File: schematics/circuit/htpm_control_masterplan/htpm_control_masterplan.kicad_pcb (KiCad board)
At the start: 2 copper layers, 248.9 x 185.4 mm, 380 parts, among them J1 Conn_01x08_Socket, J1 Conn_01x10_Socket, J2 Conn_01x04_Socket, J2 Conn_01x10_Socket, J3 Conn_01x08_Socket

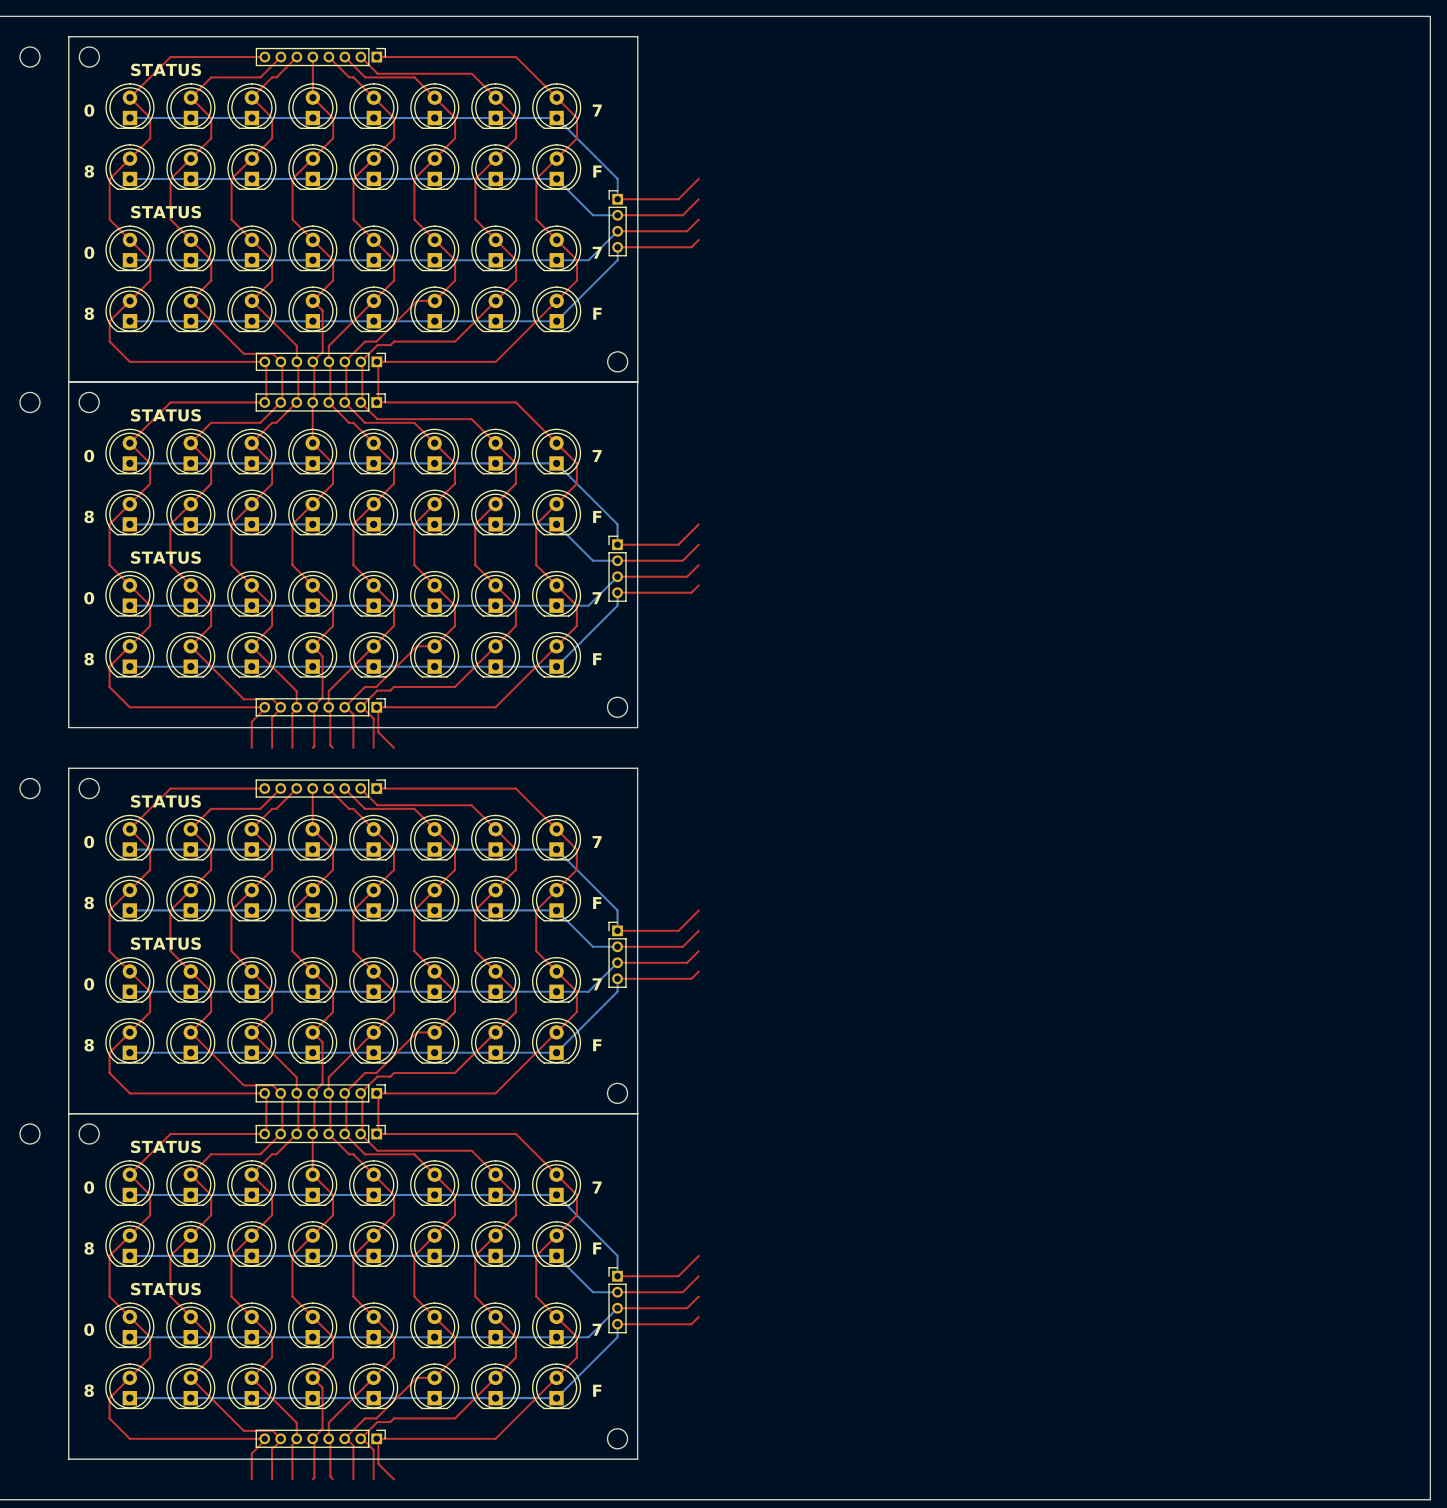
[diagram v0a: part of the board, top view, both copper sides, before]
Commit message: Added HTPm CONTROL Numericals to the masterplan.
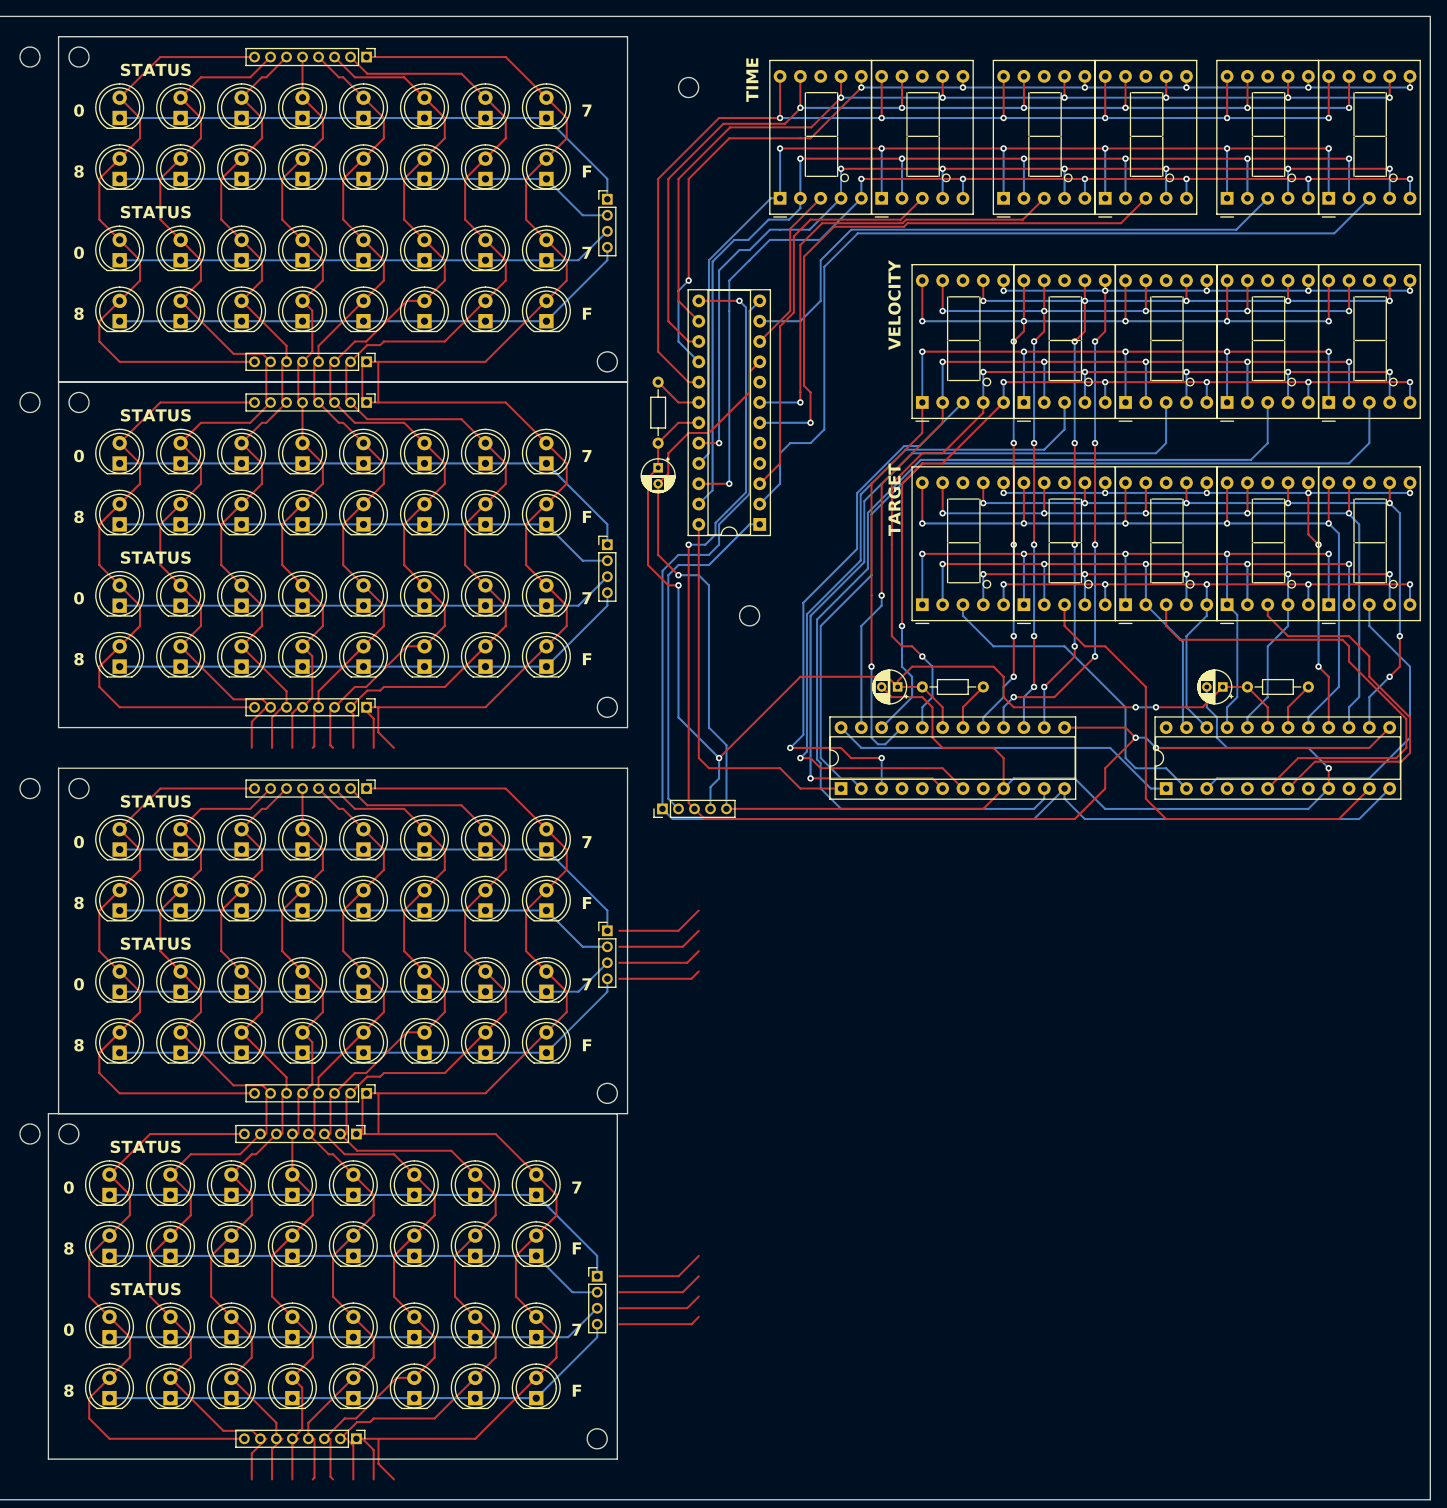
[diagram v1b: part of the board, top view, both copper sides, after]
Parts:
- added C1: 10μF, Capacitor_THT:CP_Radial_D4.0mm_P2.00mm, F.Cu at (238.8, 107.2)
- added C2: 10μF, Capacitor_THT:CP_Radial_D4.0mm_P2.00mm, F.Cu at (268.7, 134.6)
- added C3: 10μF, Capacitor_THT:CP_Radial_D4.0mm_P2.00mm, F.Cu at (309.3, 134.6)
- added H1: MountingHole, MountingHole:MountingHole_2.5mm, F.Cu at (242.6, 59.7)
- added H2: MountingHole, MountingHole:MountingHole_2.5mm, F.Cu at (250.2, 125.7)
- added J1: Conn_01x05_Socket, Connector_PinHeader_2.00mm:PinHeader_1x05_P2.00mm_Vertical, F.Cu at (239.3, 149.9)
- added R1: 15kΩ, Resistor_THT:R_Axial_DIN0204_L3.6mm_D1.6mm_P7.62mm_Horizontal, F.Cu at (238.8, 104.1)
- added R2: 15kΩ, Resistor_THT:R_Axial_DIN0204_L3.6mm_D1.6mm_P7.62mm_Horizontal, F.Cu at (271.8, 134.6)
- added R3: 15kΩ, Resistor_THT:R_Axial_DIN0204_L3.6mm_D1.6mm_P7.62mm_Horizontal, F.Cu at (312.4, 134.6)
- added U1: MAX7219, Package_DIP:DIP-24_W7.62mm_Socket, F.Cu at (251.5, 114.3)
- added U10: D168K, Display_7Segment:D1X8K, F.Cu at (297.2, 99.1)
- added U11: D168K, Display_7Segment:D1X8K, F.Cu at (309.9, 99.1)
- added U12: D168K, Display_7Segment:D1X8K, F.Cu at (322.6, 99.1)
- added U13: MAX7219, Package_DIP:DIP-24_W7.62mm_Socket, F.Cu at (261.6, 147.3)
- added U14: D168K, Display_7Segment:D1X8K, F.Cu at (322.6, 124.3)
- added U15: D168K, Display_7Segment:D1X8K, F.Cu at (309.9, 124.3)
- added U16: D168K, Display_7Segment:D1X8K, F.Cu at (297.2, 124.3)
- added U17: D168K, Display_7Segment:D1X8K, F.Cu at (284.5, 124.3)
- added U18: MAX7219, Package_DIP:DIP-24_W7.62mm_Socket, F.Cu at (302.3, 147.3)
- added U19: D168K, Display_7Segment:D1X8K, F.Cu at (271.8, 124.3)
- added U2: D168K, Display_7Segment:D1X8K, F.Cu at (254.0, 73.5)
- added U3: D168K, Display_7Segment:D1X8K, F.Cu at (266.7, 73.5)
- added U4: D168K, Display_7Segment:D1X8K, F.Cu at (281.9, 73.5)
- added U5: D168K, Display_7Segment:D1X8K, F.Cu at (294.6, 73.5)
- added U6: D168K, Display_7Segment:D1X8K, F.Cu at (309.9, 73.5)
- added U7: D168K, Display_7Segment:D1X8K, F.Cu at (322.6, 73.5)
- added U8: D168K, Display_7Segment:D1X8K, F.Cu at (271.8, 99.1)
- added U9: D168K, Display_7Segment:D1X8K, F.Cu at (284.5, 99.1)
- moved D11 2.54 mm to (185.4, 205.7)
- moved D12 2.54 mm to (193.0, 205.7)
- moved D19 2.54 mm to (185.4, 215.9)
- moved D20 2.54 mm to (193.0, 215.9)
- moved D27 2.54 mm to (185.4, 223.5)
- moved D28 2.54 mm to (193.0, 223.5)
- moved D3 2.54 mm to (185.4, 198.1)
- moved D4 2.54 mm to (193.0, 198.1)
- moved H2 2.54 mm to (231.1, 228.6)
- moved J1 2.54 mm to (201.0, 190.5)
- moved J2 2.54 mm to (231.1, 208.3)
- moved J3 2.54 mm to (201.0, 228.6)
- moved D1 2.54 mm to (170.2, 198.1)
- moved D10 2.54 mm to (177.8, 205.7)
- moved D13 2.54 mm to (200.7, 205.7)
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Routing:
- net (no net): track 8966.2 -> 13677.3 mm, vias 36 -> 211
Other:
- outline, holes or cut-outs redrawn
- board text added: "HTP!m CONTROL Numericals by shawnd.xyz"
- board text added: "TARGET"
- board text added: "TIME"
- board text added: "VELOCITY"

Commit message: Updated masterplan.
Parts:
- removed the C1 at (238.8, 107.2)
- removed the C2 at (268.7, 134.6)
- removed the C3 at (309.3, 134.6)
- removed the D1 at (171.4, 63.5)
- removed the D1 at (119.6, 106.7)
- removed the D1 at (170.2, 198.1)
- removed the D1 at (171.4, 106.7)
- removed the D1 at (119.6, 198.1)
- removed the D1 at (171.4, 154.9)
- removed the D1 at (119.6, 63.5)
- removed the D1 at (119.6, 154.9)
- removed the D10 at (177.8, 205.7)
- removed the D10 at (152.6, 160.0)
- removed the D10 at (152.6, 111.8)
- removed the D10 at (152.6, 203.2)
- removed the D10 at (179.1, 162.6)
- removed the D10 at (179.1, 114.3)
- removed the D10 at (152.6, 68.6)
- removed the D10 at (179.1, 71.1)
- removed the D11 at (186.7, 71.1)
- removed the D11 at (129.8, 81.3)
- removed the D11 at (129.8, 215.9)
- removed the D11 at (129.8, 124.5)
- removed the D11 at (186.7, 114.3)
- removed the D11 at (129.8, 172.7)
- removed the D11 at (185.4, 205.7)
- removed the D11 at (186.7, 162.6)
- removed the D12 at (137.4, 215.9)
- removed the D12 at (193.0, 205.7)
- removed the D12 at (137.4, 172.7)
- removed the D12 at (137.4, 81.3)
- removed the D12 at (137.4, 124.5)
- removed the D12 at (194.3, 162.6)
- removed the D12 at (194.3, 71.1)
- removed the D12 at (194.3, 114.3)
- removed the D13 at (145.0, 124.5)
- removed the D13 at (145.0, 81.3)
- removed the D13 at (145.0, 215.9)
- removed the D13 at (145.0, 172.7)
- removed the D13 at (201.9, 114.3)
- removed the D13 at (201.9, 71.1)
- removed the D13 at (201.9, 162.6)
- removed the D13 at (200.7, 205.7)
- removed the D14 at (208.3, 205.7)
- removed the D14 at (209.6, 162.6)
- removed the D14 at (209.6, 114.3)
- removed the D14 at (209.6, 71.1)
- removed the D14 at (152.6, 172.7)
- removed the D14 at (152.6, 81.3)
- removed the D14 at (152.6, 215.9)
- removed the D14 at (152.6, 124.5)
- removed the D15 at (129.8, 221.0)
- removed the D15 at (217.2, 71.1)
- removed the D15 at (217.2, 114.3)
- removed the D15 at (129.8, 177.8)
- removed the D15 at (215.9, 205.7)
- removed the D15 at (217.2, 162.6)
- removed the D15 at (129.8, 86.4)
- removed the D15 at (129.8, 129.5)
- removed the D16 at (224.8, 71.1)
- removed the D16 at (224.8, 114.3)
- removed the D16 at (137.4, 129.5)
- removed the D16 at (137.4, 221.0)
- removed the D16 at (223.5, 205.7)
- removed the D16 at (137.4, 86.4)
- removed the D16 at (224.8, 162.6)
- removed the D16 at (137.4, 177.8)
- removed the D17 at (145.0, 86.4)
- removed the D17 at (171.4, 172.7)
- removed the D17 at (171.4, 81.3)
- removed the D17 at (145.0, 129.5)
- removed the D17 at (170.2, 215.9)
- removed the D17 at (171.4, 124.5)
- removed the D17 at (145.0, 221.0)
- removed the D17 at (145.0, 177.8)
- removed the D18 at (179.1, 172.7)
- removed the D18 at (177.8, 215.9)
- removed the D18 at (179.1, 81.3)
- removed the D18 at (152.6, 86.4)
- removed the D18 at (152.6, 177.8)
- removed the D18 at (152.6, 129.5)
- removed the D18 at (179.1, 124.5)
- removed the D18 at (152.6, 221.0)
- removed the D19 at (186.7, 81.3)
- removed the D19 at (185.4, 215.9)
- removed the D19 at (186.7, 172.7)
- removed the D19 at (186.7, 124.5)
- removed the D2 at (119.6, 81.3)
- removed the D2 at (179.1, 154.9)
- removed the D2 at (119.6, 124.5)
- removed the D2 at (179.1, 63.5)
- removed the D2 at (119.6, 172.7)
- removed the D2 at (179.1, 106.7)
- removed the D2 at (177.8, 198.1)
- removed the D2 at (119.6, 215.9)
- removed the D20 at (194.3, 172.7)
- removed the D20 at (194.3, 124.5)
- removed the D20 at (194.3, 81.3)
- removed the D20 at (193.0, 215.9)
- removed the D21 at (201.9, 172.7)
- removed the D21 at (200.7, 215.9)
- removed the D21 at (201.9, 81.3)
- removed the D21 at (201.9, 124.5)
- removed the D22 at (209.6, 124.5)
- removed the D22 at (208.3, 215.9)
- removed the D22 at (209.6, 81.3)
- removed the D22 at (209.6, 172.7)
- removed the D23 at (217.2, 81.3)
- removed the D23 at (215.9, 215.9)
- removed the D23 at (217.2, 124.5)
- removed the D23 at (217.2, 172.7)
- removed the D24 at (224.8, 81.3)
- removed the D24 at (224.8, 172.7)
- removed the D24 at (223.5, 215.9)
- removed the D24 at (224.8, 124.5)
- removed the D25 at (170.2, 223.5)
- removed the D25 at (171.4, 88.9)
- removed the D25 at (171.4, 132.1)
- removed the D25 at (171.4, 180.3)
- removed the D26 at (179.1, 180.3)
- removed the D26 at (179.1, 88.9)
- removed the D26 at (177.8, 223.5)
- removed the D26 at (179.1, 132.1)
- removed the D27 at (186.7, 88.9)
- removed the D27 at (185.4, 223.5)
- removed the D27 at (186.7, 132.1)
- removed the D27 at (186.7, 180.3)
- removed the D28 at (194.3, 132.1)
- removed the D28 at (193.0, 223.5)
- removed the D28 at (194.3, 180.3)
- removed the D28 at (194.3, 88.9)
- removed the D29 at (201.9, 180.3)
- removed the D29 at (201.9, 132.1)
- removed the D29 at (201.9, 88.9)
- removed the D29 at (200.7, 223.5)
- removed the D3 at (129.8, 154.9)
- removed the D3 at (186.7, 63.5)
- removed the D3 at (129.8, 63.5)
- removed the D3 at (129.8, 106.7)
- removed the D3 at (129.8, 198.1)
- removed the D3 at (186.7, 154.9)
- removed the D3 at (185.4, 198.1)
- removed the D3 at (186.7, 106.7)
- removed the D30 at (208.3, 223.5)
- removed the D30 at (209.6, 132.1)
- removed the D30 at (209.6, 88.9)
- removed the D30 at (209.6, 180.3)
- removed the D31 at (217.2, 88.9)
- removed the D31 at (217.2, 180.3)
- removed the D31 at (217.2, 132.1)
- removed the D31 at (215.9, 223.5)
- removed the D32 at (224.8, 180.3)
- removed the D32 at (224.8, 132.1)
- removed the D32 at (224.8, 88.9)
- removed the D32 at (223.5, 223.5)
- removed the D4 at (137.4, 154.9)
- removed the D4 at (137.4, 63.5)
- removed the D4 at (194.3, 154.9)
- removed the D4 at (194.3, 63.5)
- removed the D4 at (193.0, 198.1)
- removed the D4 at (194.3, 106.7)
- removed the D4 at (137.4, 198.1)
- removed the D4 at (137.4, 106.7)
- removed the D5 at (201.9, 154.9)
- removed the D5 at (145.0, 198.1)
- removed the D5 at (145.0, 154.9)
- removed the D5 at (145.0, 63.5)
- removed the D5 at (145.0, 106.7)
- removed the D5 at (200.7, 198.1)
- removed the D5 at (201.9, 106.7)
- removed the D5 at (201.9, 63.5)
- removed the D6 at (152.6, 154.9)
- removed the D6 at (209.6, 154.9)
- removed the D6 at (152.6, 198.1)
- removed the D6 at (208.3, 198.1)
- removed the D6 at (209.6, 106.7)
- removed the D6 at (209.6, 63.5)
- removed the D6 at (152.6, 63.5)
- removed the D6 at (152.6, 106.7)
- removed the D7 at (217.2, 63.5)
- removed the D7 at (129.8, 68.6)
- removed the D7 at (129.8, 160.0)
- removed the D7 at (215.9, 198.1)
- removed the D7 at (217.2, 154.9)
- removed the D7 at (129.8, 111.8)
- removed the D7 at (217.2, 106.7)
- removed the D7 at (129.8, 203.2)
- removed the D8 at (224.8, 106.7)
- removed the D8 at (137.4, 68.6)
- removed the D8 at (223.5, 198.1)
- removed the D8 at (137.4, 160.0)
- removed the D8 at (137.4, 203.2)
- removed the D8 at (137.4, 111.8)
- removed the D8 at (224.8, 154.9)
- removed the D8 at (224.8, 63.5)
- removed the D9 at (145.0, 160.0)
- removed the D9 at (170.2, 205.7)
- removed the D9 at (145.0, 203.2)
- removed the D9 at (171.4, 114.3)
- removed the D9 at (171.4, 162.6)
- removed the D9 at (145.0, 111.8)
- removed the D9 at (145.0, 68.6)
- removed the D9 at (171.4, 71.1)
- removed the H1 at (166.4, 55.9)
- removed the H1 at (165.1, 190.5)
- removed the H1 at (160.2, 99.1)
- removed the H1 at (166.4, 147.3)
- removed the H1 at (166.4, 99.1)
- removed the H1 at (160.2, 190.5)
- removed the H1 at (160.2, 147.3)
- removed the H1 at (242.6, 59.7)
- removed the H1 at (160.2, 55.9)
- removed the H2 at (250.2, 125.7)
- removed the H2 at (232.4, 94.0)
- removed the H2 at (129.8, 137.2)
- removed the H2 at (129.8, 185.4)
- removed the H2 at (129.8, 228.6)
- removed the H2 at (232.4, 137.2)
- removed the H2 at (231.1, 228.6)
- removed the H2 at (232.4, 185.4)
- removed the H2 at (129.8, 94.0)
- removed the J1 at (201.0, 190.5)
- removed the J1 at (202.3, 99.1)
- removed the J1 at (202.3, 55.9)
- removed the J1 at (109.4, 137.2)
- removed the J1 at (202.3, 147.3)
- removed the J1 at (109.4, 185.4)
- removed the J1 at (109.4, 228.6)
- removed the J1 at (109.4, 94.0)
- removed the J1 at (239.3, 149.9)
- removed the J2 at (109.4, 99.1)
- removed the J2 at (232.4, 73.7)
- removed the J2 at (109.4, 55.9)
- removed the J2 at (109.4, 190.5)
- removed the J2 at (232.4, 165.1)
- removed the J2 at (109.4, 147.3)
- removed the J2 at (231.1, 208.3)
- removed the J2 at (232.4, 116.8)
- removed the J3 at (202.3, 137.2)
- removed the J3 at (201.0, 228.6)
- removed the J3 at (202.3, 94.0)
- removed the J3 at (202.3, 185.4)
- removed the JP1 at (106.9, 113.6)
- removed the JP1 at (106.9, 161.8)
- removed the JP1 at (106.9, 70.4)
- removed the JP1 at (106.9, 205.0)
- removed the JP10 at (106.9, 174.5)
- removed the JP10 at (106.9, 126.3)
- removed the JP10 at (106.9, 217.7)
- removed the JP10 at (106.9, 83.1)
- removed the JP11 at (109.4, 174.5)
- removed the JP11 at (109.4, 217.7)
- removed the JP11 at (109.4, 126.3)
- removed the JP11 at (109.4, 83.1)
- removed the JP12 at (112.0, 217.7)
- removed the JP12 at (112.0, 126.3)
- removed the JP12 at (112.0, 83.1)
- removed the JP12 at (112.0, 174.5)
- removed the JP13 at (104.4, 130.3)
- removed the JP13 at (104.4, 221.7)
- removed the JP13 at (104.4, 87.1)
- removed the JP13 at (104.4, 178.5)
- removed the JP14 at (106.9, 221.7)
- removed the JP14 at (106.9, 87.1)
- removed the JP14 at (106.9, 178.5)
- removed the JP14 at (106.9, 130.3)
- removed the JP15 at (109.4, 178.5)
- removed the JP15 at (109.4, 87.1)
- removed the JP15 at (109.4, 130.3)
- removed the JP15 at (109.4, 221.7)
- removed the JP16 at (112.0, 87.1)
- removed the JP16 at (112.0, 130.3)
- removed the JP16 at (112.0, 221.7)
- removed the JP16 at (112.0, 178.5)
- removed the JP17 at (101.1, 195.6)
- removed the JP17 at (101.1, 61.0)
- removed the JP17 at (101.1, 104.1)
- removed the JP17 at (101.1, 152.4)
- removed the JP18 at (101.1, 106.7)
- removed the JP18 at (101.1, 198.1)
- removed the JP18 at (101.1, 63.5)
- removed the JP18 at (101.1, 154.9)
- removed the JP19 at (101.1, 157.5)
- removed the JP19 at (101.1, 200.7)
- removed the JP19 at (101.1, 66.0)
- removed the JP19 at (101.1, 109.2)
- removed the JP2 at (109.4, 70.4)
- removed the JP2 at (109.4, 161.8)
- removed the JP2 at (109.4, 113.6)
- removed the JP2 at (109.4, 205.0)
- removed the JP20 at (101.1, 111.8)
- removed the JP20 at (101.1, 203.2)
- removed the JP20 at (101.1, 68.6)
- removed the JP20 at (101.1, 160.0)
- removed the JP21 at (101.1, 71.1)
- removed the JP21 at (101.1, 162.6)
- removed the JP21 at (101.1, 114.3)
- removed the JP21 at (101.1, 205.7)
- removed the JP22 at (101.1, 208.3)
- removed the JP22 at (101.1, 116.8)
- removed the JP22 at (101.1, 73.7)
- removed the JP22 at (101.1, 165.1)
- removed the JP23 at (101.1, 210.8)
- removed the JP23 at (101.1, 119.4)
- removed the JP23 at (101.1, 76.2)
- removed the JP23 at (101.1, 167.6)
- removed the JP24 at (101.1, 121.9)
- removed the JP24 at (101.1, 213.4)
- removed the JP24 at (101.1, 78.7)
- removed the JP24 at (101.1, 170.2)
- removed the JP25 at (93.5, 78.7)
- removed the JP25 at (93.5, 213.4)
- removed the JP25 at (93.5, 121.9)
- removed the JP25 at (93.5, 170.2)
- removed the JP26 at (93.5, 167.6)
- removed the JP26 at (93.5, 119.4)
- removed the JP26 at (93.5, 76.2)
- removed the JP26 at (93.5, 210.8)
- removed the JP27 at (93.5, 208.3)
- removed the JP27 at (93.5, 165.1)
- removed the JP27 at (93.5, 116.8)
- removed the JP27 at (93.5, 73.7)
- removed the JP28 at (93.5, 162.6)
- removed the JP28 at (93.5, 205.7)
- removed the JP28 at (93.5, 71.1)
- removed the JP28 at (93.5, 114.3)
- removed the JP29 at (93.5, 203.2)
- removed the JP29 at (93.5, 111.8)
- removed the JP29 at (93.5, 160.0)
- removed the JP29 at (93.5, 68.6)
- removed the JP3 at (112.0, 70.4)
- removed the JP3 at (112.0, 161.8)
- removed the JP3 at (112.0, 205.0)
- removed the JP3 at (112.0, 113.6)
- removed the JP30 at (93.5, 157.5)
- removed the JP30 at (93.5, 109.2)
- removed the JP30 at (93.5, 66.0)
- removed the JP30 at (93.5, 200.7)
- removed the JP31 at (93.5, 154.9)
- removed the JP31 at (93.5, 106.7)
- removed the JP31 at (93.5, 63.5)
- removed the JP31 at (93.5, 198.1)
- removed the JP32 at (93.5, 152.4)
- removed the JP32 at (93.5, 61.0)
- removed the JP32 at (93.5, 195.6)
- removed the JP32 at (93.5, 104.1)
- removed the JP4 at (114.5, 161.8)
- removed the JP4 at (114.5, 205.0)
- removed the JP4 at (114.5, 113.6)
- removed the JP4 at (114.5, 70.4)
- removed the JP5 at (106.9, 74.4)
- removed the JP5 at (106.9, 209.0)
- removed the JP5 at (106.9, 117.6)
- removed the JP5 at (106.9, 165.8)
- removed the JP6 at (109.4, 74.4)
- removed the JP6 at (109.4, 209.0)
- removed the JP6 at (109.4, 165.8)
- removed the JP6 at (109.4, 117.6)
- removed the JP7 at (112.0, 74.4)
- removed the JP7 at (112.0, 209.0)
- removed the JP7 at (112.0, 165.8)
- removed the JP7 at (112.0, 117.6)
- removed the JP8 at (114.5, 209.0)
- removed the JP8 at (114.5, 74.4)
- removed the JP8 at (114.5, 165.8)
- removed the JP8 at (114.5, 117.6)
- removed the JP9 at (104.4, 174.5)
- removed the JP9 at (104.4, 217.7)
- removed the JP9 at (104.4, 83.1)
- removed the JP9 at (104.4, 126.3)
- removed the R1 at (238.8, 104.1)
- removed the R1 at (105.6, 104.1)
- removed the R1 at (105.6, 61.0)
- removed the R1 at (105.6, 195.6)
- removed the R1 at (105.6, 152.4)
- removed the R2 at (106.9, 213.4)
- removed the R2 at (106.9, 78.7)
- removed the R2 at (106.9, 170.2)
- removed the R2 at (271.8, 134.6)
- removed the R2 at (106.9, 121.9)
- removed the R3 at (90.4, 175.3)
- removed the R3 at (312.4, 134.6)
- removed the R3 at (90.4, 127.0)
- removed the R3 at (90.4, 83.8)
- removed the R3 at (90.4, 218.4)
- removed the R4 at (105.6, 66.0)
- removed the R4 at (105.6, 109.2)
- removed the R4 at (105.6, 157.5)
- removed the R4 at (105.6, 200.7)
- removed the U1 at (251.5, 114.3)
- removed the U2 at (254.0, 73.5)
- removed the U3 at (266.7, 73.5)
- removed the U4 at (281.9, 73.5)
- removed the U5 at (294.6, 73.5)
- removed the U6 at (309.9, 73.5)
- removed the U7 at (322.6, 73.5)
- added C1: 22μF, Capacitor_THT:CP_Radial_D4.0mm_P2.00mm, F.Cu at (332.0, 228.1)
- added C1: 10μF, Capacitor_THT:CP_Radial_D4.0mm_P2.00mm, F.Cu at (238.8, 104.8)
- added C2: 10μF, Capacitor_THT:CP_Radial_D4.0mm_P2.00mm, F.Cu at (268.7, 132.2)
- added C2: 22μF, Capacitor_THT:CP_Radial_D4.0mm_P2.00mm, F.Cu at (309.4, 228.1)
- added C3: 22μF, Capacitor_THT:CP_Radial_D4.0mm_P2.00mm, F.Cu at (267.5, 210.3)
- added C3: 10μF, Capacitor_THT:CP_Radial_D4.0mm_P2.00mm, F.Cu at (309.3, 132.2)
- added C4: 22μF, Capacitor_THT:CP_Radial_D4.0mm_P2.00mm, F.Cu at (330.7, 154.7)
- added C5: 10μF, Capacitor_THT:CP_Radial_D4.0mm_P2.00mm, F.Cu at (258.8, 165.6)
- added C6: 10μF, Capacitor_THT:CP_Radial_D4.0mm_P2.00mm, F.Cu at (258.1, 192.3)
- added D1: LED, LED_THT:LED_D5.0mm, F.Cu at (170.2, 147.3)
- added D1: RED, LED_THT:LED_D5.0mm, F.Cu at (116.8, 61.0)
- added D1: RED, LED_THT:LED_D5.0mm, F.Cu at (276.9, 156.5)
- added D1: LED, LED_THT:LED_D5.0mm, F.Cu at (170.2, 61.0)
- added D1: RED, LED_THT:LED_D5.0mm, F.Cu at (116.8, 147.3)
- added D1: LED, LED_THT:LED_D5.0mm, F.Cu at (170.2, 104.1)
- added D1: RED, LED_THT:LED_D5.0mm, F.Cu at (116.8, 190.5)
- added D1: RED, LED_THT:LED_D5.0mm, F.Cu at (116.8, 104.1)
- added D1: LED, LED_THT:LED_D5.0mm, F.Cu at (170.2, 190.5)
- added D10: LED, LED_THT:LED_D5.0mm, F.Cu at (177.8, 111.8)
- added D10: BLUE, LED_THT:LED_D5.0mm, F.Cu at (149.9, 195.6)
- added D10: YELLOW, LED_THT:LED_D5.0mm, F.Cu at (292.1, 190.5)
- added D10: LED, LED_THT:LED_D5.0mm, F.Cu at (177.8, 154.9)
- added D10: BLUE, LED_THT:LED_D5.0mm, F.Cu at (149.9, 109.2)
- added D10: BLUE, LED_THT:LED_D5.0mm, F.Cu at (149.9, 152.4)
- added D10: LED, LED_THT:LED_D5.0mm, F.Cu at (177.8, 68.6)
- added D10: LED, LED_THT:LED_D5.0mm, F.Cu at (177.8, 198.1)
- added D10: BLUE, LED_THT:LED_D5.0mm, F.Cu at (149.9, 66.0)
- added D11: LED, LED_THT:LED_D5.0mm, F.Cu at (185.4, 68.6)
- added D11: BLUE, LED_THT:LED_D5.0mm, F.Cu at (127.0, 165.1)
- added D11: BLUE, LED_THT:LED_D5.0mm, F.Cu at (127.0, 121.9)
- added D11: BLUE, LED_THT:LED_D5.0mm, F.Cu at (127.0, 78.7)
- added D11: BLUE, LED_THT:LED_D5.0mm, F.Cu at (127.0, 208.3)
- added D11: YELLOW, LED_THT:LED_D5.0mm, F.Cu at (284.5, 190.5)
- added D11: LED, LED_THT:LED_D5.0mm, F.Cu at (185.4, 198.1)
- added D11: LED, LED_THT:LED_D5.0mm, F.Cu at (185.4, 111.8)
- added D11: LED, LED_THT:LED_D5.0mm, F.Cu at (185.4, 154.9)
- added D12: BLUE, LED_THT:LED_D5.0mm, F.Cu at (134.6, 121.9)
- added D12: BLUE, LED_THT:LED_D5.0mm, F.Cu at (134.6, 165.1)
- added D12: BLUE, LED_THT:LED_D5.0mm, F.Cu at (134.6, 208.3)
- added D12: LED, LED_THT:LED_D5.0mm, F.Cu at (193.1, 154.9)
- added D12: BLUE, LED_THT:LED_D5.0mm, F.Cu at (134.6, 78.7)
- added D12: LED, LED_THT:LED_D5.0mm, F.Cu at (193.1, 198.1)
- added D12: YELLOW, LED_THT:LED_D5.0mm, F.Cu at (276.9, 190.5)
- added D12: LED, LED_THT:LED_D5.0mm, F.Cu at (193.0, 68.6)
- added D12: LED, LED_THT:LED_D5.0mm, F.Cu at (193.1, 111.8)
- added D13: BLUE, LED_THT:LED_D5.0mm, F.Cu at (142.2, 121.9)
- added D13: BLUE, LED_THT:LED_D5.0mm, F.Cu at (142.2, 78.7)
- added D13: BLUE, LED_THT:LED_D5.0mm, F.Cu at (142.2, 165.1)
- added D13: YELLOW, LED_THT:LED_D5.0mm, F.Cu at (330.2, 195.6)
- added D13: LED, LED_THT:LED_D5.0mm, F.Cu at (200.7, 68.6)
- added D13: LED, LED_THT:LED_D5.0mm, F.Cu at (200.7, 154.9)
- added D13: BLUE, LED_THT:LED_D5.0mm, F.Cu at (142.2, 208.3)
- added D13: LED, LED_THT:LED_D5.0mm, F.Cu at (200.7, 198.1)
- added D13: LED, LED_THT:LED_D5.0mm, F.Cu at (200.7, 111.8)
- added D14: BLUE, LED_THT:LED_D5.0mm, F.Cu at (149.9, 78.7)
- added D14: BLUE, LED_THT:LED_D5.0mm, F.Cu at (149.9, 165.1)
- added D14: LED, LED_THT:LED_D5.0mm, F.Cu at (208.3, 68.6)
- added D14: LED, LED_THT:LED_D5.0mm, F.Cu at (208.3, 154.9)
- added D14: YELLOW, LED_THT:LED_D5.0mm, F.Cu at (322.6, 195.6)
- added D14: LED, LED_THT:LED_D5.0mm, F.Cu at (208.3, 198.1)
- added D14: BLUE, LED_THT:LED_D5.0mm, F.Cu at (149.9, 121.9)
- added D14: LED, LED_THT:LED_D5.0mm, F.Cu at (208.3, 111.8)
- added D14: BLUE, LED_THT:LED_D5.0mm, F.Cu at (149.9, 208.3)
- added D15: LED, LED_THT:LED_D5.0mm, F.Cu at (215.9, 68.6)
- added D15: BLUE, LED_THT:LED_D5.0mm, F.Cu at (127.0, 83.8)
- added D15: LED, LED_THT:LED_D5.0mm, F.Cu at (215.9, 198.1)
- added D15: LED, LED_THT:LED_D5.0mm, F.Cu at (215.9, 154.9)
- added D15: BLUE, LED_THT:LED_D5.0mm, F.Cu at (127.0, 170.2)
- added D15: BLUE, LED_THT:LED_D5.0mm, F.Cu at (127.0, 127.0)
- added D15: BLUE, LED_THT:LED_D5.0mm, F.Cu at (127.0, 213.4)
- added D15: YELLOW, LED_THT:LED_D5.0mm, F.Cu at (315.0, 195.6)
- added D15: LED, LED_THT:LED_D5.0mm, F.Cu at (215.9, 111.8)
- added D16: LED, LED_THT:LED_D5.0mm, F.Cu at (223.5, 154.9)
- added D16: LED, LED_THT:LED_D5.0mm, F.Cu at (223.5, 111.8)
- added D16: BLUE, LED_THT:LED_D5.0mm, F.Cu at (134.6, 127.0)
- added D16: YELLOW, LED_THT:LED_D5.0mm, F.Cu at (307.3, 195.6)
- added D16: BLUE, LED_THT:LED_D5.0mm, F.Cu at (134.6, 83.8)
- added D16: LED, LED_THT:LED_D5.0mm, F.Cu at (223.5, 68.6)
- added D16: LED, LED_THT:LED_D5.0mm, F.Cu at (223.5, 198.1)
- added D16: BLUE, LED_THT:LED_D5.0mm, F.Cu at (134.6, 170.2)
- added D16: BLUE, LED_THT:LED_D5.0mm, F.Cu at (134.6, 213.4)
- added D17: BLUE, LED_THT:LED_D5.0mm, F.Cu at (142.2, 127.0)
- added D17: LED, LED_THT:LED_D5.0mm, F.Cu at (170.2, 78.7)
- added D17: BLUE, LED_THT:LED_D5.0mm, F.Cu at (142.2, 213.4)
- added D17: LED, LED_THT:LED_D5.0mm, F.Cu at (170.2, 208.3)
- added D17: BLUE, LED_THT:LED_D5.0mm, F.Cu at (142.2, 83.8)
- added D17: YELLOW, LED_THT:LED_D5.0mm, F.Cu at (299.7, 195.6)
- added D17: BLUE, LED_THT:LED_D5.0mm, F.Cu at (142.2, 170.2)
- added D17: LED, LED_THT:LED_D5.0mm, F.Cu at (170.2, 121.9)
- added D17: LED, LED_THT:LED_D5.0mm, F.Cu at (170.2, 165.1)
- added D18: LED, LED_THT:LED_D5.0mm, F.Cu at (177.8, 78.7)
- added D18: BLUE, LED_THT:LED_D5.0mm, F.Cu at (149.9, 83.8)
- added D18: BLUE, LED_THT:LED_D5.0mm, F.Cu at (149.9, 213.4)
- added D18: YELLOW, LED_THT:LED_D5.0mm, F.Cu at (292.1, 195.6)
- added D18: LED, LED_THT:LED_D5.0mm, F.Cu at (177.8, 165.1)
- added D18: BLUE, LED_THT:LED_D5.0mm, F.Cu at (149.9, 127.0)
- added D18: LED, LED_THT:LED_D5.0mm, F.Cu at (177.8, 208.3)
- added D18: LED, LED_THT:LED_D5.0mm, F.Cu at (177.8, 121.9)
- added D18: BLUE, LED_THT:LED_D5.0mm, F.Cu at (149.9, 170.2)
- added D19: LED, LED_THT:LED_D5.0mm, F.Cu at (185.4, 208.3)
- added D19: YELLOW, LED_THT:LED_D5.0mm, F.Cu at (284.5, 195.6)
- added D19: LED, LED_THT:LED_D5.0mm, F.Cu at (185.4, 121.9)
- added D19: LED, LED_THT:LED_D5.0mm, F.Cu at (185.4, 165.1)
- added D19: LED, LED_THT:LED_D5.0mm, F.Cu at (185.4, 78.7)
- added D2: RED, LED_THT:LED_D5.0mm, F.Cu at (116.8, 121.9)
- added D2: LED, LED_THT:LED_D5.0mm, F.Cu at (177.8, 147.3)
- added D2: LED, LED_THT:LED_D5.0mm, F.Cu at (177.8, 104.1)
- added D2: LED, LED_THT:LED_D5.0mm, F.Cu at (177.8, 190.5)
- added D2: LED, LED_THT:LED_D5.0mm, F.Cu at (177.8, 61.0)
- added D2: RED, LED_THT:LED_D5.0mm, F.Cu at (116.8, 208.3)
- added D2: RED, LED_THT:LED_D5.0mm, F.Cu at (116.8, 78.7)
- added D2: RED, LED_THT:LED_D5.0mm, F.Cu at (116.8, 165.1)
- added D2: RED, LED_THT:LED_D5.0mm, F.Cu at (276.9, 164.1)
- added D20: LED, LED_THT:LED_D5.0mm, F.Cu at (193.0, 78.7)
- added D20: LED, LED_THT:LED_D5.0mm, F.Cu at (193.1, 208.3)
- added D20: LED, LED_THT:LED_D5.0mm, F.Cu at (193.1, 165.1)
- added D20: LED, LED_THT:LED_D5.0mm, F.Cu at (193.1, 121.9)
- added D20: YELLOW, LED_THT:LED_D5.0mm, F.Cu at (276.9, 195.6)
- added D21: LED, LED_THT:LED_D5.0mm, F.Cu at (200.7, 121.9)
- added D21: LED, LED_THT:LED_D5.0mm, F.Cu at (200.7, 165.1)
- added D21: LED, LED_THT:LED_D5.0mm, F.Cu at (200.7, 78.7)
- added D21: LED, LED_THT:LED_D5.0mm, F.Cu at (200.7, 208.3)
- added D22: LED, LED_THT:LED_D5.0mm, F.Cu at (208.3, 165.1)
- added D22: LED, LED_THT:LED_D5.0mm, F.Cu at (208.3, 78.7)
- added D22: LED, LED_THT:LED_D5.0mm, F.Cu at (208.3, 121.9)
- added D22: LED, LED_THT:LED_D5.0mm, F.Cu at (208.3, 208.3)
- added D23: LED, LED_THT:LED_D5.0mm, F.Cu at (215.9, 165.1)
- added D23: LED, LED_THT:LED_D5.0mm, F.Cu at (215.9, 78.7)
- added D23: LED, LED_THT:LED_D5.0mm, F.Cu at (215.9, 121.9)
- added D23: LED, LED_THT:LED_D5.0mm, F.Cu at (215.9, 208.3)
- added D24: LED, LED_THT:LED_D5.0mm, F.Cu at (223.5, 208.3)
- added D24: LED, LED_THT:LED_D5.0mm, F.Cu at (223.5, 121.9)
- added D24: LED, LED_THT:LED_D5.0mm, F.Cu at (223.5, 165.1)
- added D24: LED, LED_THT:LED_D5.0mm, F.Cu at (223.5, 78.7)
- added D25: LED, LED_THT:LED_D5.0mm, F.Cu at (170.2, 172.7)
- added D25: LED, LED_THT:LED_D5.0mm, F.Cu at (170.2, 86.4)
- added D25: LED, LED_THT:LED_D5.0mm, F.Cu at (170.2, 129.5)
- added D25: LED, LED_THT:LED_D5.0mm, F.Cu at (170.2, 215.9)
- added D26: LED, LED_THT:LED_D5.0mm, F.Cu at (177.8, 129.5)
- added D26: LED, LED_THT:LED_D5.0mm, F.Cu at (177.8, 215.9)
- added D26: LED, LED_THT:LED_D5.0mm, F.Cu at (177.8, 86.4)
- added D26: LED, LED_THT:LED_D5.0mm, F.Cu at (177.8, 172.7)
- added D27: LED, LED_THT:LED_D5.0mm, F.Cu at (185.4, 129.5)
- added D27: LED, LED_THT:LED_D5.0mm, F.Cu at (185.4, 215.9)
- added D27: LED, LED_THT:LED_D5.0mm, F.Cu at (185.4, 172.7)
- added D27: LED, LED_THT:LED_D5.0mm, F.Cu at (185.4, 86.4)
- added D28: LED, LED_THT:LED_D5.0mm, F.Cu at (193.1, 172.7)
- added D28: LED, LED_THT:LED_D5.0mm, F.Cu at (193.1, 215.9)
- added D28: LED, LED_THT:LED_D5.0mm, F.Cu at (193.1, 129.5)
- added D28: LED, LED_THT:LED_D5.0mm, F.Cu at (193.0, 86.4)
- added D29: LED, LED_THT:LED_D5.0mm, F.Cu at (200.7, 172.7)
- added D29: LED, LED_THT:LED_D5.0mm, F.Cu at (200.7, 215.9)
- added D29: LED, LED_THT:LED_D5.0mm, F.Cu at (200.7, 129.5)
- added D29: LED, LED_THT:LED_D5.0mm, F.Cu at (200.7, 86.4)
- added D3: BLUE, LED_THT:LED_D5.0mm, F.Cu at (127.0, 61.0)
- added D3: LED, LED_THT:LED_D5.0mm, F.Cu at (185.4, 104.1)
- added D3: BLUE, LED_THT:LED_D5.0mm, F.Cu at (127.0, 147.3)
- added D3: GREEN, LED_THT:LED_D5.0mm, F.Cu at (276.9, 171.7)
- added D3: BLUE, LED_THT:LED_D5.0mm, F.Cu at (127.0, 190.5)
- added D3: LED, LED_THT:LED_D5.0mm, F.Cu at (185.4, 61.0)
- added D3: BLUE, LED_THT:LED_D5.0mm, F.Cu at (127.0, 104.1)
- added D3: LED, LED_THT:LED_D5.0mm, F.Cu at (185.4, 190.5)
- added D3: LED, LED_THT:LED_D5.0mm, F.Cu at (185.4, 147.3)
- added D30: LED, LED_THT:LED_D5.0mm, F.Cu at (208.3, 172.7)
- added D30: LED, LED_THT:LED_D5.0mm, F.Cu at (208.3, 129.5)
- added D30: LED, LED_THT:LED_D5.0mm, F.Cu at (208.3, 215.9)
- added D30: LED, LED_THT:LED_D5.0mm, F.Cu at (208.3, 86.4)
- added D31: LED, LED_THT:LED_D5.0mm, F.Cu at (215.9, 172.7)
- added D31: LED, LED_THT:LED_D5.0mm, F.Cu at (215.9, 215.9)
- added D31: LED, LED_THT:LED_D5.0mm, F.Cu at (215.9, 129.5)
- added D31: LED, LED_THT:LED_D5.0mm, F.Cu at (215.9, 86.4)
- added D32: LED, LED_THT:LED_D5.0mm, F.Cu at (223.5, 172.7)
- added D32: LED, LED_THT:LED_D5.0mm, F.Cu at (223.5, 129.5)
- added D32: LED, LED_THT:LED_D5.0mm, F.Cu at (223.5, 86.4)
- added D32: LED, LED_THT:LED_D5.0mm, F.Cu at (223.5, 215.9)
- added D4: LED, LED_THT:LED_D5.0mm, F.Cu at (193.0, 61.0)
- added D4: LED, LED_THT:LED_D5.0mm, F.Cu at (193.1, 190.5)
- added D4: BLUE, LED_THT:LED_D5.0mm, F.Cu at (134.6, 147.3)
- added D4: BLUE, LED_THT:LED_D5.0mm, F.Cu at (134.6, 61.0)
- added D4: BLUE, LED_THT:LED_D5.0mm, F.Cu at (134.6, 104.1)
- added D4: BLUE, LED_THT:LED_D5.0mm, F.Cu at (134.6, 190.5)
- added D4: YELLOW, LED_THT:LED_D5.0mm, F.Cu at (276.9, 179.3)
- added D4: LED, LED_THT:LED_D5.0mm, F.Cu at (193.1, 147.3)
- added D4: LED, LED_THT:LED_D5.0mm, F.Cu at (193.1, 104.1)
- added D5: LED, LED_THT:LED_D5.0mm, F.Cu at (200.7, 61.0)
- added D5: YELLOW, LED_THT:LED_D5.0mm, F.Cu at (330.2, 190.5)
- added D5: BLUE, LED_THT:LED_D5.0mm, F.Cu at (142.2, 61.0)
- added D5: LED, LED_THT:LED_D5.0mm, F.Cu at (200.7, 104.1)
- added D5: BLUE, LED_THT:LED_D5.0mm, F.Cu at (142.2, 190.5)
- added D5: LED, LED_THT:LED_D5.0mm, F.Cu at (200.7, 190.5)
- added D5: BLUE, LED_THT:LED_D5.0mm, F.Cu at (142.2, 104.1)
- added D5: BLUE, LED_THT:LED_D5.0mm, F.Cu at (142.2, 147.3)
- added D5: LED, LED_THT:LED_D5.0mm, F.Cu at (200.7, 147.3)
- added D6: LED, LED_THT:LED_D5.0mm, F.Cu at (208.3, 190.5)
- added D6: LED, LED_THT:LED_D5.0mm, F.Cu at (208.3, 147.3)
- added D6: BLUE, LED_THT:LED_D5.0mm, F.Cu at (149.9, 61.0)
- added D6: LED, LED_THT:LED_D5.0mm, F.Cu at (208.3, 104.1)
- added D6: BLUE, LED_THT:LED_D5.0mm, F.Cu at (149.9, 190.5)
- added D6: YELLOW, LED_THT:LED_D5.0mm, F.Cu at (322.6, 190.5)
- added D6: BLUE, LED_THT:LED_D5.0mm, F.Cu at (149.9, 147.3)
- added D6: LED, LED_THT:LED_D5.0mm, F.Cu at (208.3, 61.0)
- added D6: BLUE, LED_THT:LED_D5.0mm, F.Cu at (149.9, 104.1)
- added D7: LED, LED_THT:LED_D5.0mm, F.Cu at (215.9, 190.5)
- added D7: LED, LED_THT:LED_D5.0mm, F.Cu at (215.9, 104.1)
- added D7: LED, LED_THT:LED_D5.0mm, F.Cu at (215.9, 147.3)
- added D7: BLUE, LED_THT:LED_D5.0mm, F.Cu at (127.0, 195.6)
- added D7: LED, LED_THT:LED_D5.0mm, F.Cu at (215.9, 61.0)
- added D7: BLUE, LED_THT:LED_D5.0mm, F.Cu at (127.0, 152.4)
- added D7: YELLOW, LED_THT:LED_D5.0mm, F.Cu at (315.0, 190.5)
- added D7: BLUE, LED_THT:LED_D5.0mm, F.Cu at (127.0, 66.0)
- added D7: BLUE, LED_THT:LED_D5.0mm, F.Cu at (127.0, 109.2)
- added D8: BLUE, LED_THT:LED_D5.0mm, F.Cu at (134.6, 109.2)
- added D8: LED, LED_THT:LED_D5.0mm, F.Cu at (223.5, 190.5)
- added D8: BLUE, LED_THT:LED_D5.0mm, F.Cu at (134.6, 152.4)
- added D8: BLUE, LED_THT:LED_D5.0mm, F.Cu at (134.6, 66.0)
- added D8: LED, LED_THT:LED_D5.0mm, F.Cu at (223.5, 147.3)
- added D8: LED, LED_THT:LED_D5.0mm, F.Cu at (223.5, 104.1)
- added D8: YELLOW, LED_THT:LED_D5.0mm, F.Cu at (307.3, 190.5)
- added D8: BLUE, LED_THT:LED_D5.0mm, F.Cu at (134.6, 195.6)
- added D8: LED, LED_THT:LED_D5.0mm, F.Cu at (223.5, 61.0)
- added D9: BLUE, LED_THT:LED_D5.0mm, F.Cu at (142.2, 109.2)
- added D9: LED, LED_THT:LED_D5.0mm, F.Cu at (170.2, 68.6)
- added D9: LED, LED_THT:LED_D5.0mm, F.Cu at (170.2, 154.9)
- added D9: LED, LED_THT:LED_D5.0mm, F.Cu at (170.2, 111.8)
- added D9: BLUE, LED_THT:LED_D5.0mm, F.Cu at (142.2, 66.0)
- added D9: BLUE, LED_THT:LED_D5.0mm, F.Cu at (142.2, 152.4)
- added D9: LED, LED_THT:LED_D5.0mm, F.Cu at (170.2, 198.1)
- added D9: BLUE, LED_THT:LED_D5.0mm, F.Cu at (142.2, 195.6)
- added D9: YELLOW, LED_THT:LED_D5.0mm, F.Cu at (299.7, 190.5)
- added H1: MountingHole, MountingHole:MountingHole_2.5mm, F.Cu at (157.5, 139.7)
- added H1: MountingHole, MountingHole:MountingHole_2.5mm, F.Cu at (157.5, 96.5)
- added H1: MountingHole, MountingHole:MountingHole_2.5mm, F.Cu at (242.6, 57.3)
- added H1: MountingHole, MountingHole:MountingHole_2.5mm, F.Cu at (165.1, 53.3)
- added H1: MountingHole, MountingHole:MountingHole_2.5mm, F.Cu at (157.5, 53.3)
- added H1: MountingHole, MountingHole:MountingHole_2.5mm, F.Cu at (165.1, 182.9)
- added H1: MountingHole, MountingHole:MountingHole_2.5mm, F.Cu at (165.1, 96.5)
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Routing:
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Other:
- outline, holes or cut-outs redrawn
- board text added: "4"
- board text added: "ACCELERATE"
- board text added: "Controller"
- board text added: "DECELERATE"
- board text added: "DP"
- board text added: "EMERGENCY STOP"
- board text added: "HTP!m CONTROL Additional Info by shawnd.xyz"
- board text added: "Module Display"
- board text added: "Numericals"
- board text added: "OVERRIDE"
- board text added: "Status A"
- board text added: "Status B"

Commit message: Updated HTPm CONTROL masterplan.
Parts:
- moved C6 0.26 mm to (258.1, 192.5)
- moved D4 0.26 mm to (276.8, 179.6)
- moved J1 0.26 mm to (262.6, 229.6)
- moved J6 0.26 mm to (238.7, 188.5)
- moved J7 0.26 mm to (238.7, 198.6)
- moved J8 0.26 mm to (254.8, 229.6)
- moved R1 0.26 mm to (306.3, 159.3)
- moved R22 0.26 mm to (265.1, 208.0)
- moved U2 0.26 mm to (332.0, 215.7)
- moved U3 0.26 mm to (309.3, 215.7)
- moved U7 0.26 mm to (270.5, 197.1)
- moved C5 0.26 mm to (258.8, 165.9)
- moved D10 0.26 mm to (292.1, 190.8)
- moved D17 0.26 mm to (299.7, 195.8)
- moved D18 0.26 mm to (292.1, 195.8)
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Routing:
- net (no net): track 16280.6 -> 20620.4 mm
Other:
- outline, holes or cut-outs redrawn
- board text added: "To the Main Circuit"
